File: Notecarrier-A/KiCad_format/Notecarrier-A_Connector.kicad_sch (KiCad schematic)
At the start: 48 parts, among them J13 BM04B-SRSS-TBT, J14 BM04B-SRSS-TBT, J20 MDT420E01001, J5 NanoSIM - SF72S006VBAR2500, J7 uFL-R-SMT-1-10, J8 uFL-R-SMT-1-10, Q2 AO3420, U5 BGA725L6E6327FTSA1

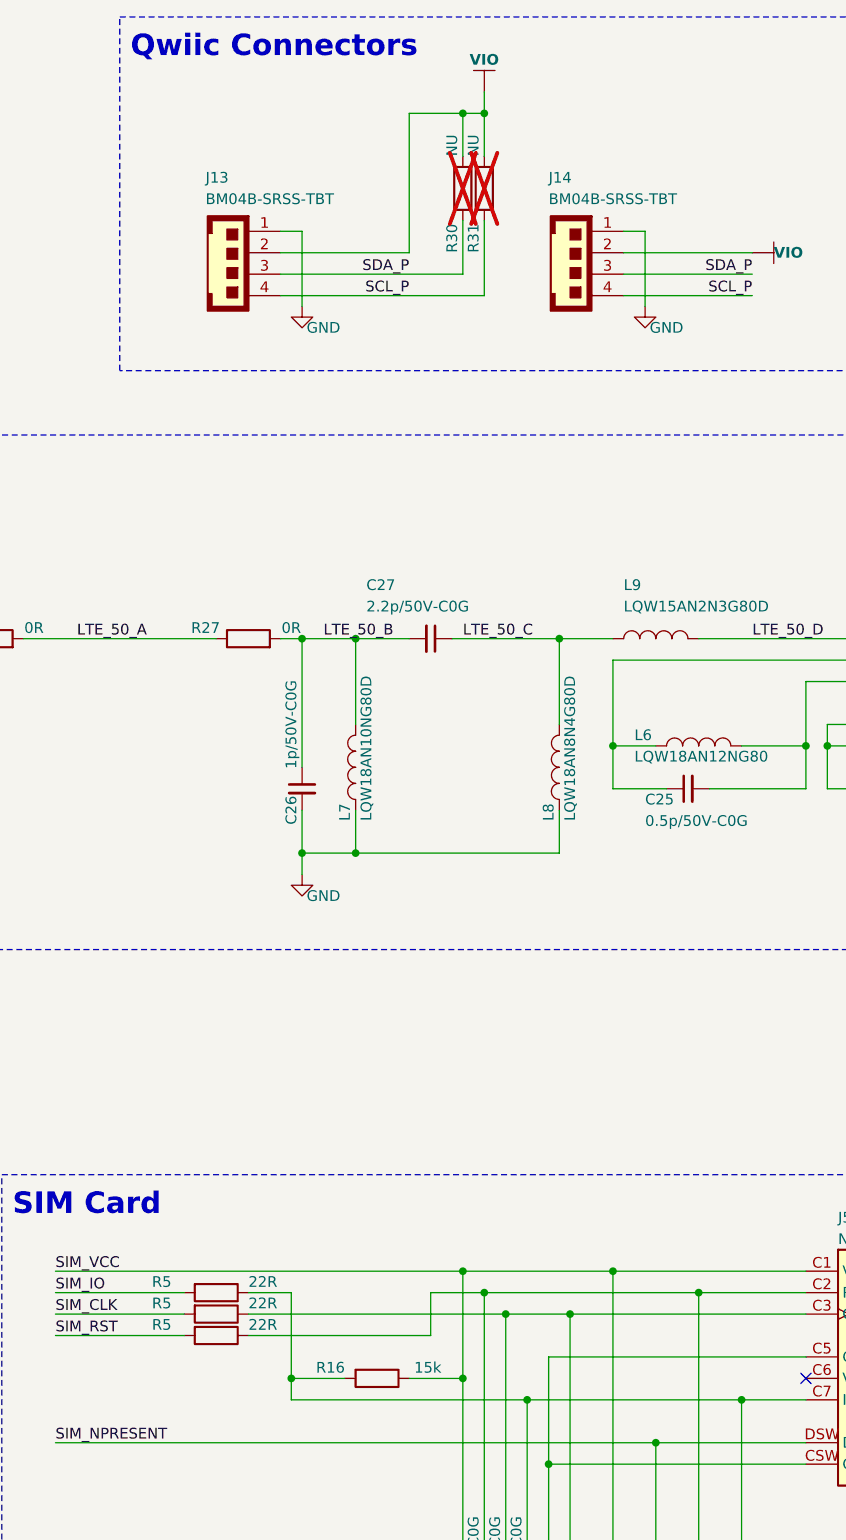
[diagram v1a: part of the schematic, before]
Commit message: First pass port of Notecarrier-B PCB.
See PortingNotes for details. To go: 3D models and validation.
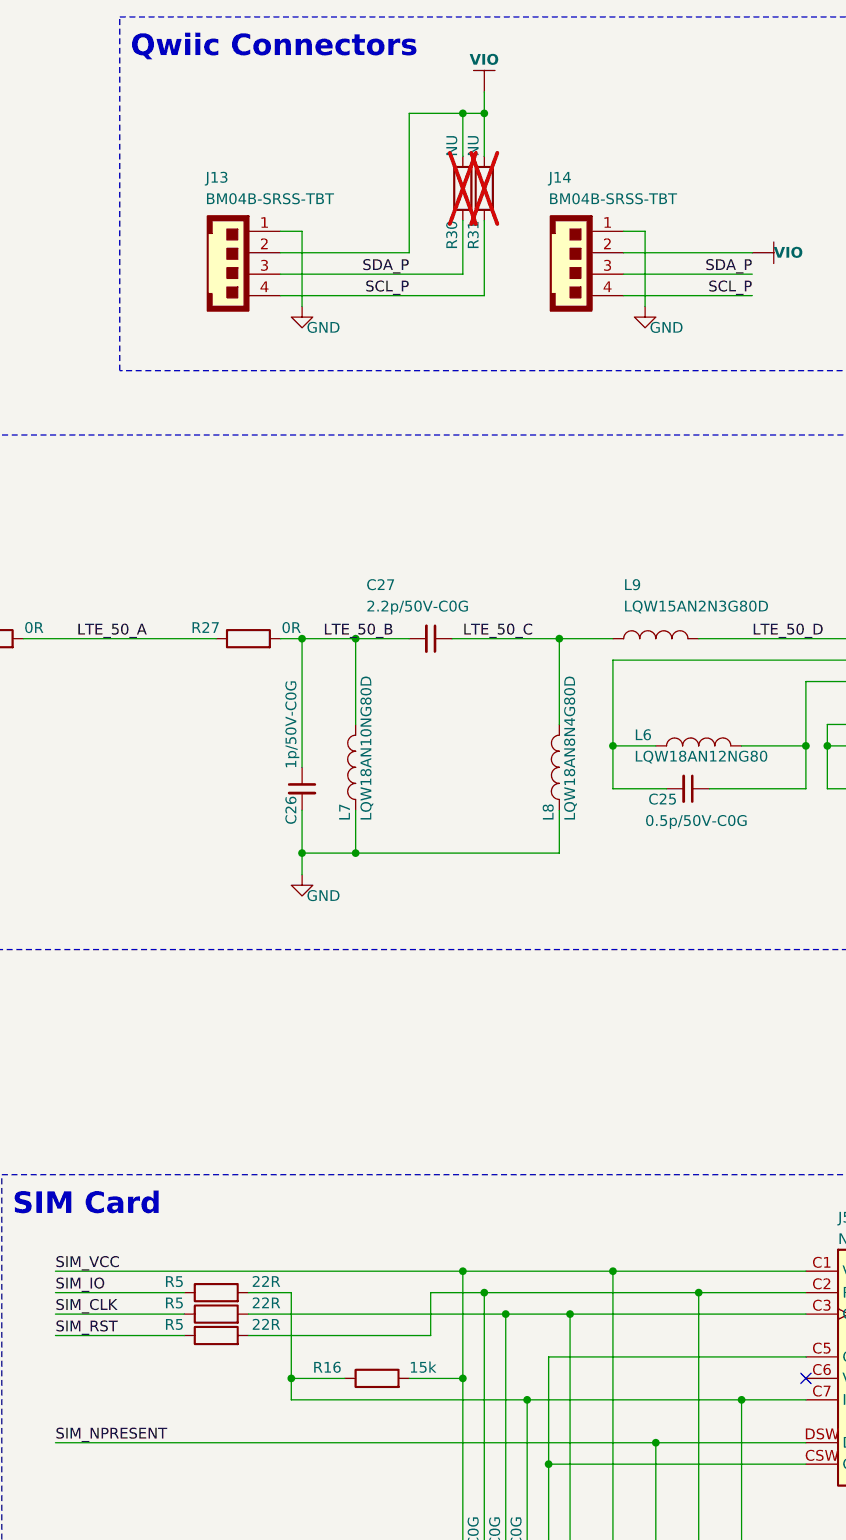
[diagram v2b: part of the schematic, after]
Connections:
- net SCL_P: now also R31.1; no longer R31.2
- net SDA_P: now also R30.1; no longer R30.2
- net SIM_CLK: now also R5.1; no longer R5.2
- net SIM_IO: now also R5.1; no longer R5.2
- net SIM_RST: now also R5.1; no longer R5.2
- net SIM_VCC: now also R16.2; no longer R16.1
- net VIO: now also R30.2, R31.2; no longer R30.1, R31.1
- net at C3.1, J5.C3 (CLK), TVS2.1 (K1): now also R5.2; no longer R5.1
- net at C3.1, J5.C2 (RST), TVS2.5 (K4): now also R5.2; no longer R5.1
- net at C3.1, J5.C7 (I/O), TVS2.6 (K5): now also R16.1, R5.2; no longer R16.2, R5.1
- net at ANT1.2 (MN1-A), L6.1: now also C25.2; no longer C25.1
- net at ANT1.3 (MN1-B), L6.2: now also C25.1; no longer C25.2
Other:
- moved on the sheet: C25, R16, R30, R31, R5
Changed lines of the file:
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@@
     )
   )
-  (symbol (lib_id "Device:R") (at 273.05 170.18 270) (unit 1)
-    (in_bom yes) (on_board yes) (dnp no)
-    (property "Reference" "R5" (at 265.43 168.91 90)
-      (effects (font (size 1.27 1.27)) (justify left))
-    )
-    (property "Value" "22R" (at 276.86 168.91 90)
-      (effects (font (size 1.27 1.27)) (justify left))
-    )
-    (property "Footprint" "blues-kicad-lib:RS-0603" (at 273.05 168.402 90)
+  (symbol (lib_id "Device:R") (at 273.05 170.18 90) (unit 1)
+    (in_bom yes) (on_board yes) (dnp no)
+    (property "Reference" "R5" (at 269.24 168.91 90)
+      (effects (font (size 1.27 1.27)) (justify left))
+    )
+    (property "Value" "22R" (at 280.67 168.91 90)
+      (effects (font (size 1.27 1.27)) (justify left))
+    )
+    (property "Footprint" "blues-kicad-lib:RS-0603" (at 273.05 171.958 90)
       (effects (font (size 1.27 1.27)) hide)
     )
@@
     )
   )
-  (symbol (lib_id "Device:R") (at 304.8 39.37 0) (unit 1)
+  (symbol (lib_id "Device:R") (at 304.8 39.37 180) (unit 1)
     (in_bom yes) (on_board yes) (dnp yes)
-    (property "Reference" "R31" (at 303.53 46.99 90)
-      (effects (font (size 1.27 1.27)) (justify left))
-    )
-    (property "Value" "NU" (at 303.53 35.56 90)
-      (effects (font (size 1.27 1.27)) (justify left))
-    )
-    (property "Footprint" "blues-kicad-lib:RS-0603" (at 303.022 39.37 90)
+    (property "Reference" "R31" (at 303.53 43.18 90)
+      (effects (font (size 1.27 1.27)) (justify left))
+    )
+    (property "Value" "NU" (at 303.53 33.02 90)
+      (effects (font (size 1.27 1.27)) (justify left))
+    )
+    (property "Footprint" "blues-kicad-lib:RS-0603" (at 306.578 39.37 90)
       (effects (font (size 1.27 1.27)) hide)
     )
@@
     )
   )
-  (symbol (lib_id "Device:R") (at 273.05 175.26 270) (unit 1)
-    (in_bom yes) (on_board yes) (dnp no)
-    (property "Reference" "R5" (at 265.43 173.99 90)
-      (effects (font (size 1.27 1.27)) (justify left))
-    )
-    (property "Value" "22R" (at 276.86 173.99 90)
-      (effects (font (size 1.27 1.27)) (justify left))
-    )
-    (property "Footprint" "blues-kicad-lib:RS-0603" (at 273.05 173.482 90)
+  (symbol (lib_id "Device:R") (at 273.05 175.26 90) (unit 1)
+    (in_bom yes) (on_board yes) (dnp no)
+    (property "Reference" "R5" (at 269.24 173.99 90)
+      (effects (font (size 1.27 1.27)) (justify left))
+    )
+    (property "Value" "22R" (at 280.67 173.99 90)
+      (effects (font (size 1.27 1.27)) (justify left))
+    )
+    (property "Footprint" "blues-kicad-lib:RS-0603" (at 273.05 177.038 90)
       (effects (font (size 1.27 1.27)) hide)
     )
@@
     )
   )
-  (symbol (lib_id "Device:R") (at 292.1 180.34 270) (unit 1)
-    (in_bom yes) (on_board yes) (dnp no)
-    (property "Reference" "R16" (at 288.29 179.07 90)
+  (symbol (lib_id "Device:R") (at 292.1 180.34 90) (unit 1)
+    (in_bom yes) (on_board yes) (dnp no)
+    (property "Reference" "R16" (at 284.48 179.07 90)
       (effects (font (size 1.27 1.27)) (justify right))
     )
-    (property "Value" "15k" (at 299.72 179.07 90)
+    (property "Value" "15k" (at 295.91 179.07 90)
       (effects (font (size 1.27 1.27)) (justify right))
     )
-    (property "Footprint" "blues-kicad-lib:RS-0402" (at 292.1 178.562 90)
+    (property "Footprint" "blues-kicad-lib:RS-0402" (at 292.1 182.118 90)
       (effects (font (size 1.27 1.27)) hide)
     )
@@
     )
   )
-  (symbol (lib_id "Device:R") (at 302.26 39.37 0) (unit 1)
+  (symbol (lib_id "Device:R") (at 302.26 39.37 180) (unit 1)
     (in_bom yes) (on_board yes) (dnp yes)
-    (property "Reference" "R30" (at 300.99 46.99 90)
-      (effects (font (size 1.27 1.27)) (justify left))
-    )
-    (property "Value" "NU" (at 300.99 35.56 90)
-      (effects (font (size 1.27 1.27)) (justify left))
-    )
-    (property "Footprint" "blues-kicad-lib:RS-0603" (at 300.482 39.37 90)
+    (property "Reference" "R30" (at 300.99 43.18 90)
+      (effects (font (size 1.27 1.27)) (justify left))
+    )
+    (property "Value" "NU" (at 300.99 33.02 90)
+      (effects (font (size 1.27 1.27)) (justify left))
+    )
+    (property "Footprint" "blues-kicad-lib:RS-0603" (at 304.038 39.37 90)
       (effects (font (size 1.27 1.27)) hide)
     )
@@
     )
   )
-  (symbol (lib_id "Device:R") (at 273.05 172.72 270) (unit 1)
-    (in_bom yes) (on_board yes) (dnp no)
-    (property "Reference" "R5" (at 265.43 171.45 90)
-      (effects (font (size 1.27 1.27)) (justify left))
-    )
-    (property "Value" "22R" (at 276.86 171.45 90)
-      (effects (font (size 1.27 1.27)) (justify left))
-    )
-    (property "Footprint" "blues-kicad-lib:RS-0603" (at 273.05 170.942 90)
+  (symbol (lib_id "Device:R") (at 273.05 172.72 90) (unit 1)
+    (in_bom yes) (on_board yes) (dnp no)
+    (property "Reference" "R5" (at 269.24 171.45 90)
+      (effects (font (size 1.27 1.27)) (justify left))
+    )
+    (property "Value" "22R" (at 280.67 171.45 90)
+      (effects (font (size 1.27 1.27)) (justify left))
+    )
+    (property "Footprint" "blues-kicad-lib:RS-0603" (at 273.05 174.498 90)
       (effects (font (size 1.27 1.27)) hide)
     )
@@
     )
   )
-  (symbol (lib_id "Device:C_Small") (at 328.93 110.49 90) (unit 1)
-    (in_bom yes) (on_board yes) (dnp no)
-    (property "Reference" "C25" (at 323.85 111.76 90)
+  (symbol (lib_id "Device:C_Small") (at 328.93 110.49 270) (unit 1)
+    (in_bom yes) (on_board yes) (dnp no)
+    (property "Reference" "C25" (at 327.66 111.76 90)
       (effects (font (size 1.27 1.27)) (justify right))
     )
     (property "Value" "0.5p/50V-C0G" (at 323.85 114.3 90)
-      (effects (font (size 1.27 1.27)) (justify right))
+      (effects (font (size 1.27 1.27)) (justify left))
     )
     (property "Footprint" "blues-kicad-lib:FRACTUS-0404_NO-SILK" (at 328.93 110.49 0)

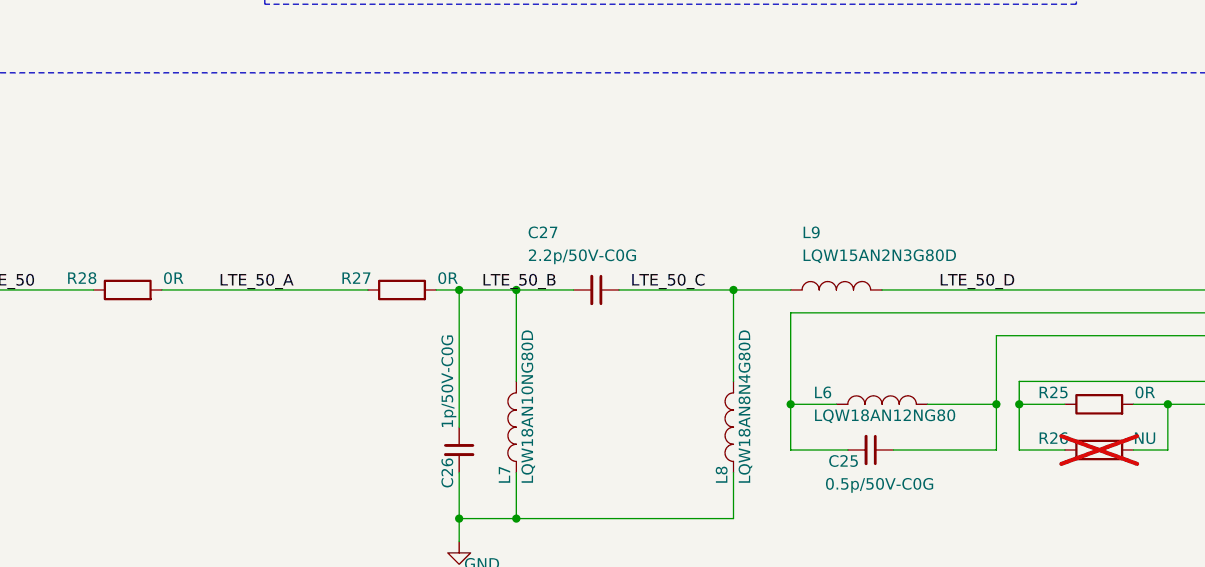
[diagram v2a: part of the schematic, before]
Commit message: Release RevA of Notecarrier-A port.
Validation complete. Results in the validation directory, documented in PortingNotes.md.
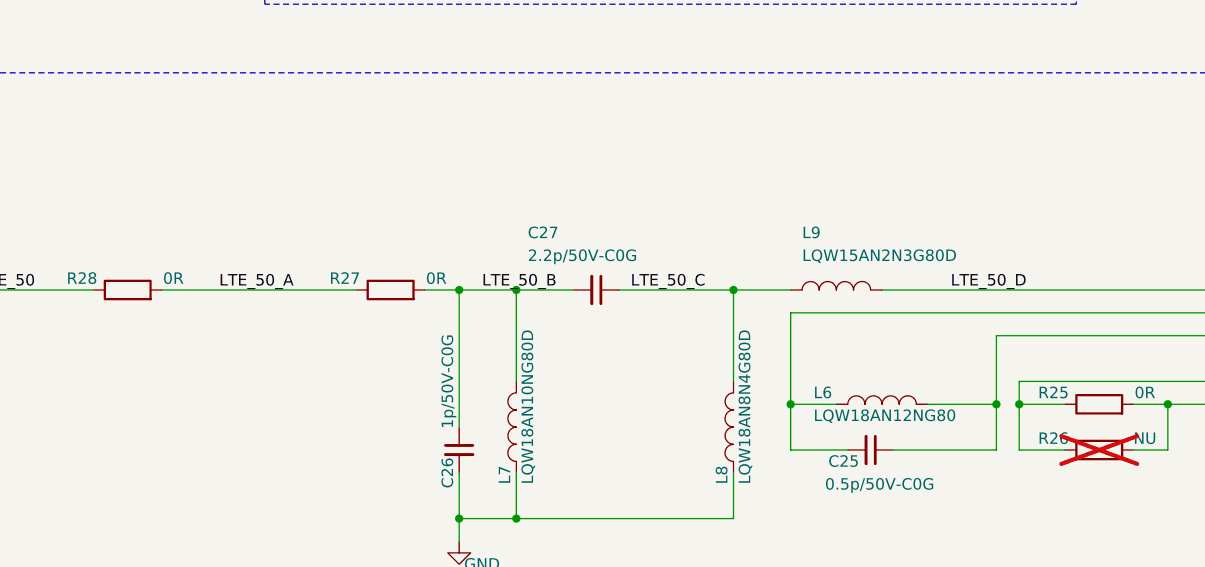
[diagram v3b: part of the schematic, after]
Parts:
- J20: footprint blues-kicad-lib:J-75-0050-MOS-M2-E -> blues-kicad-lib:J-75-0050-MOS-M2-E_smaller-mask
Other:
- moved on the sheet: R27
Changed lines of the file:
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@@
   (title_block
     (title "Notecarrier-A")
-    (date "DRAFT")
+    (date "2023-05-23")
     (rev "A")
     (comment 1 "Blues Inc")
@@
     (stroke (width 0) (type default))
   )
-  (wire (pts (xy 280.67 92.71) (xy 283.21 92.71))
+  (wire (pts (xy 279.4 92.71) (xy 283.21 92.71))
     (stroke (width 0) (type default))
   )
@@
     (stroke (width 0.6) (type default) (color 0 0 0 1))
   )
-  (wire (pts (xy 250.19 92.71) (xy 273.05 92.71))
+  (wire (pts (xy 250.19 92.71) (xy 271.78 92.71))
     (stroke (width 0) (type default))
   )
@@
     (effects (font (size 1.27 1.27)) (justify right bottom))
   )
-  (label "LTE_50_D" (at 336.55 92.71 0) (fields_autoplaced)
+  (label "LTE_50_D" (at 337.82 92.71 0) (fields_autoplaced)
     (effects (font (size 1.27 1.27)) (justify left bottom))
   )
@@
       (effects (font (size 1.27 1.27)) (justify left))
     )
-    (property "Footprint" "blues-kicad-lib:J-75-0050-MOS-M2-E" (at 132.08 167.64 0)
+    (property "Footprint" "blues-kicad-lib:J-75-0050-MOS-M2-E_smaller-mask" (at 132.08 167.64 0)
       (effects (font (size 1.27 1.27)) hide)
     )
@@
     )
     (property "Distributor" "FAE" (at 129.54 114.3 0)
+      (effects (font (size 1.27 1.27)) hide)
+    )
+    (property "Critical" "" (at 129.54 114.3 0)
+      (effects (font (size 1.27 1.27)) hide)
+    )
+    (property "Manufacturer" "" (at 129.54 114.3 0)
+      (effects (font (size 1.27 1.27)) hide)
+    )
+    (property "Order Code" "" (at 129.54 114.3 0)
+      (effects (font (size 1.27 1.27)) hide)
+    )
+    (property "Part Number" "" (at 129.54 114.3 0)
+      (effects (font (size 1.27 1.27)) hide)
+    )
+    (property "Supplier" "" (at 129.54 114.3 0)
       (effects (font (size 1.27 1.27)) hide)
     )
@@
     )
   )
-  (symbol (lib_id "Device:R") (at 276.86 92.71 90) (unit 1)
+  (symbol (lib_id "Device:R") (at 275.59 92.71 90) (unit 1)
     (in_bom yes) (on_board yes) (dnp no)
-    (property "Reference" "R27" (at 271.78 91.44 90)
+    (property "Reference" "R27" (at 270.51 91.44 90)
       (effects (font (size 1.27 1.27)))
     )
-    (property "Value" "0R" (at 281.94 91.44 90)
+    (property "Value" "0R" (at 280.67 91.44 90)
       (effects (font (size 1.27 1.27)))
     )
-    (property "Footprint" "blues-kicad-lib:FRACTUS-0404_NO-SILK" (at 276.86 94.488 90)
-      (effects (font (size 1.27 1.27)) hide)
-    )
-    (property "Datasheet" "~" (at 276.86 92.71 0)
-      (effects (font (size 1.27 1.27)) hide)
-    )
-    (property "Caratteristiche" "1%" (at 276.86 92.71 0)
-      (effects (font (size 1.27 1.27)) hide)
-    )
-    (property "Description" "CHIP RES. 0R 0603 1/16W 1%" (at 276.86 92.71 0)
-      (effects (font (size 1.27 1.27)) hide)
-    )
-    (property "Pkg Type" "SMD" (at 276.86 92.71 0)
-      (effects (font (size 1.27 1.27)) hide)
-    )
-    (property "Temperature" "-55°..+150°" (at 276.86 92.71 0)
-      (effects (font (size 1.27 1.27)) hide)
-    )
-    (property "Distributor" "FAE" (at 276.86 92.71 0)
-      (effects (font (size 1.27 1.27)) hide)
-    )
+    (property "Footprint" "blues-kicad-lib:FRACTUS-0404_NO-SILK" (at 275.59 94.488 90)
+      (effects (font (size 1.27 1.27)) hide)
+    )
+    (property "Datasheet" "~" (at 275.59 92.71 0)
+      (effects (font (size 1.27 1.27)) hide)
+    )
+    (property "Caratteristiche" "1%" (at 275.59 92.71 0)
+      (effects (font (size 1.27 1.27)) hide)
+    )
+    (property "Description" "CHIP RES. 0R 0603 1/16W 1%" (at 275.59 92.71 0)
+      (effects (font (size 1.27 1.27)) hide)
+    )
+    (property "Pkg Type" "SMD" (at 275.59 92.71 0)
+      (effects (font (size 1.27 1.27)) hide)
+    )
+    (property "Temperature" "-55°..+150°" (at 275.59 92.71 0)
+      (effects (font (size 1.27 1.27)) hide)
+    )
+    (property "Distributor" "FAE" (at 275.59 92.71 0)
+      (effects (font (size 1.27 1.27)) hide)
+    )
